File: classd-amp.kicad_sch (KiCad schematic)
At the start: 50 parts, among them Q1 IRF540N, Q2 IRF540N, Q3 IRF540N, Q4 IRF540N, U1 TL072, U2 TL072, U4 LT1016, U5 IR2184, U6 IR2184

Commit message: Added right channel
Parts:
- removed C1: 22u, TerminalBlock_4Ucon:TerminalBlock_4Ucon_1x02_P3.50mm_Horizontal, symbol Device:C
- removed C10, C11, C4, C8, C9: 1n, Capacitor_THT:C_Disc_D4.7mm_W2.5mm_P5.00mm, symbol Device:C
- removed C12, C13, C14: 100n, Capacitor_THT:C_Disc_D3.4mm_W2.1mm_P2.50mm, symbol Device:C
- removed C15, C16: 1u, Capacitor_THT:CP_Radial_D4.0mm_P1.50mm, symbol Device:C_Polarized
- removed C2, C5, C6: 22u, Capacitor_THT:CP_Radial_D8.0mm_P3.50mm, symbol Device:C
- removed C21, C22: 1u, Capacitor_THT:C_Rect_L18.0mm_W11.0mm_P15.00mm_FKS3_FKP3, symbol Device:C
- removed C23, C24: 10u, Capacitor_THT:CP_Radial_D4.0mm_P1.50mm, symbol Device:C_Polarized
- removed D1, D2: 1N4001, Diode_THT:D_DO-41_SOD81_P10.16mm_Horizontal, symbol Device:D
- removed D3, D4, D5, D6: SB140, Diode_THT:D_DO-41_SOD81_P10.16mm_Horizontal, symbol Device:D_Schottky
- removed L1, L2: 33u, Inductor_THT:L_Toroid_Vertical_L17.8mm_W8.1mm_P7.62mm_Bourns_5700, symbol Device:L
- removed Q1, Q2, Q3, Q4: IRF540N, Package_TO_SOT_THT:TO-220-3_Vertical, symbol PCM_Transistor_MOSFET_AKL:IRF540N
- removed R1, R2: 22k, Resistor_THT:R_Axial_DIN0204_L3.6mm_D1.6mm_P7.62mm_Horizontal, symbol Device:R
- removed R10, R11, R12, R9: 4.7, Resistor_THT:R_Axial_DIN0204_L3.6mm_D1.6mm_P7.62mm_Horizontal, symbol Device:R
- removed R13, R14: 10, Resistor_THT:R_Axial_DIN0614_L14.3mm_D5.7mm_P5.08mm_Vertical, symbol Device:R
- removed R3, R4: 47k, Resistor_THT:R_Axial_DIN0204_L3.6mm_D1.6mm_P7.62mm_Horizontal, symbol Device:R
- removed R5, R6: 3.3k, Resistor_THT:R_Axial_DIN0204_L3.6mm_D1.6mm_P7.62mm_Horizontal, symbol Device:R
- removed R7, R8: 100k, Resistor_THT:R_Axial_DIN0204_L3.6mm_D1.6mm_P7.62mm_Horizontal, symbol Device:R
- removed RV1: 1k, Potentiometer_THT:TRIM_3362P-1-253LF, symbol Device:R_Potentiometer_Trim
- removed U1, U2: TL072, PCM_Package_DIP_AKL:DIP-8_W7.62mm, symbol Amplifier_Operational:TL072
- removed U4: LT1016, PCM_Package_DIP_AKL:DIP-8_W7.62mm, symbol Comparator:LT1016
- removed U5, U6: IR2184, PCM_Package_DIP_AKL:DIP-8_W7.62mm, symbol Driver_FET:IR2184
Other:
- added sheet Left Channel (left.kicad_sch)
- added sheet Right Channel (right.kicad_sch)

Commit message: First prototype
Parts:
- added J2: Conn_Coaxial_x2, Connector_Audio:RCA_Stereo_Connector, symbol Connector:Conn_Coaxial_x2
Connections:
- new net GND: J2.3 (EXT)
- new net LIN: J2.2 (IN2)
- new net RIN: J2.1 (IN1)
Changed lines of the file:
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@@
 (kicad_sch (version 20230121) (generator eeschema)
   (paper "A4")
+  (wire (pts (xy 22.86 81.28) (xy 27.94 81.28))
+    (stroke (width 0) (type default))
+  )
+  (wire (pts (xy 27.94 100.33) (xy 30.48 100.33))
+    (stroke (width 0) (type default))
+  )
+  (wire (pts (xy 27.94 81.28) (xy 27.94 85.09))
+    (stroke (width 0) (type default))
+  )
+  (wire (pts (xy 27.94 95.25) (xy 30.48 95.25))
+    (stroke (width 0) (type default))
+  )
+  (wire (pts (xy 22.86 90.17) (xy 22.86 81.28))
+    (stroke (width 0) (type default))
+  )
+  (global_label "LIN" (shape output) (at 30.48 95.25 0) (fields_autoplaced)
+    (effects (font (size 1.27 1.27)) (justify left))
+    (property "Intersheetrefs" "${INTERSHEET_REFS}" (at 36.4286 95.25 0)
+      (effects (font (size 1.27 1.27)) (justify left) hide)
+    )
+  )
+  (global_label "RIN" (shape output) (at 30.48 100.33 0) (fields_autoplaced)
+    (effects (font (size 1.27 1.27)) (justify left))
+    (property "Intersheetrefs" "${INTERSHEET_REFS}" (at 36.6705 100.33 0)
+      (effects (font (size 1.27 1.27)) (justify left) hide)
+    )
+  )
+  (symbol (lib_id "Connector:Conn_Coaxial_x2") (at 22.86 97.79 180) (unit 1)
+    (in_bom yes) (on_board yes) (dnp no) (fields_autoplaced)
+    (property "Reference" "J2" (at 19.05 96.2268 0)
+      (effects (font (size 1.27 1.27)) (justify left))
+    )
+    (property "Value" "Conn_Coaxial_x2" (at 19.05 98.7668 0)
+      (effects (font (size 1.27 1.27)) (justify left) hide)
+    )
+    (property "Footprint" "Connector_Audio:RCA_Stereo_Connector" (at 22.86 95.25 0)
+      (effects (font (size 1.27 1.27)) hide)
+    )
+    (property "Datasheet" " ~" (at 22.86 95.25 0)
+      (effects (font (size 1.27 1.27)) hide)
+    )
+    (pin "1")
+    (pin "2")
+    (pin "3")
+    (instances
+      (project "classd-amp"
+        (path "/4342a3a3-4383-4661-90ac-821979f46c8c"
+          (reference "J2") (unit 1)
+        )
+      )
+    )
+  )
+  (symbol (lib_id "power:GND") (at 27.94 85.09 0) (unit 1)
+    (in_bom yes) (on_board yes) (dnp no) (fields_autoplaced)
+    (property "Reference" "#PWR056" (at 27.94 91.44 0)
+      (effects (font (size 1.27 1.27)) hide)
+    )
+    (property "Value" "GND" (at 27.94 90.17 0)
+      (effects (font (size 1.27 1.27)))
+    )
+    (property "Footprint" "" (at 27.94 85.09 0)
+      (effects (font (size 1.27 1.27)) hide)
+    )
+    (property "Datasheet" "" (at 27.94 85.09 0)
+      (effects (font (size 1.27 1.27)) hide)
+    )
+    (pin "1")
+    (instances
+      (project "classd-amp"
+        (path "/4342a3a3-4383-4661-90ac-821979f46c8c"
+          (reference "#PWR056") (unit 1)
+        )
+      )
+    )
+  )
   (sheet (at 167.64 83.82) (size 110.49 69.85) (fields_autoplaced)
     (stroke (width 0.1524) (type solid))
@@
     )
   )
-  (sheet (at 39.37 115.57) (size 110.49 69.85) (fields_autoplaced)
+  (sheet (at 49.53 107.95) (size 110.49 69.85) (fields_autoplaced)
     (stroke (width 0.1524) (type solid))
     (fill (color 0 0 0 0.0000))
-    (property "Sheetname" "Left Channel" (at 39.37 114.8584 0)
+    (property "Sheetname" "Left Channel" (at 49.53 107.2384 0)
       (effects (font (size 1.27 1.27)) (justify left bottom))
     )
-    (property "Sheetfile" "left.kicad_sch" (at 39.37 186.0046 0)
+    (property "Sheetfile" "left.kicad_sch" (at 49.53 178.3846 0)
       (effects (font (size 1.27 1.27)) (justify left top))
     )
@@
     )
   )
-  (sheet (at 29.464 26.67) (size 82.296 69.85) (fields_autoplaced)
+  (sheet (at 73.914 25.4) (size 82.296 69.85) (fields_autoplaced)
     (stroke (width 0.1524) (type solid))
     (fill (color 0 0 0 0.0000))
-    (property "Sheetname" "Power Supplies" (at 29.464 25.9584 0)
+    (property "Sheetname" "Power Supplies" (at 73.914 24.6884 0)
       (effects (font (size 1.27 1.27)) (justify left bottom))
     )
-    (property "Sheetfile" "power.kicad_sch" (at 29.464 97.1046 0)
+    (property "Sheetfile" "power.kicad_sch" (at 73.914 95.8346 0)
       (effects (font (size 1.27 1.27)) (justify left top))
     )

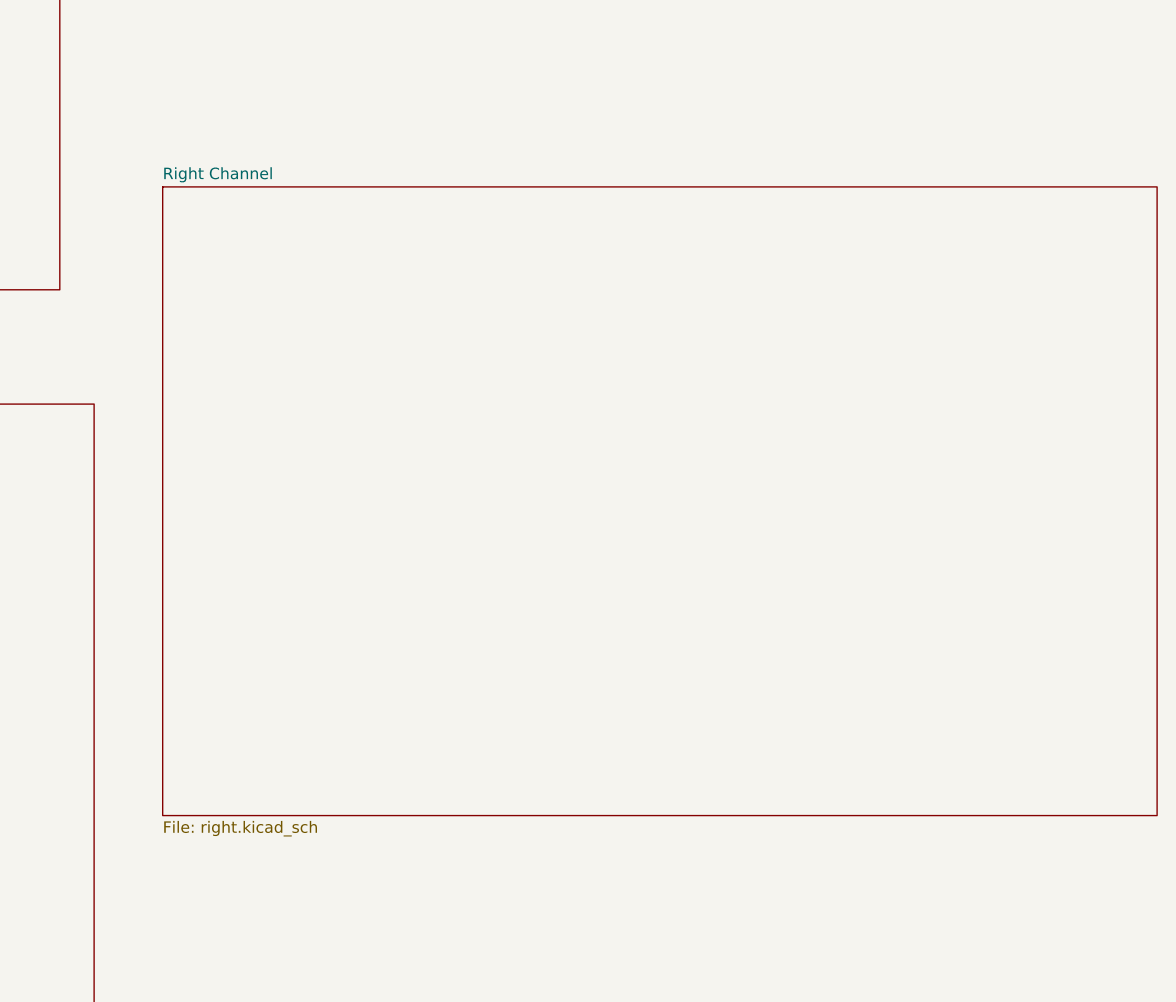
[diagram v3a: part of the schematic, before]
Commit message: Recovered PCB
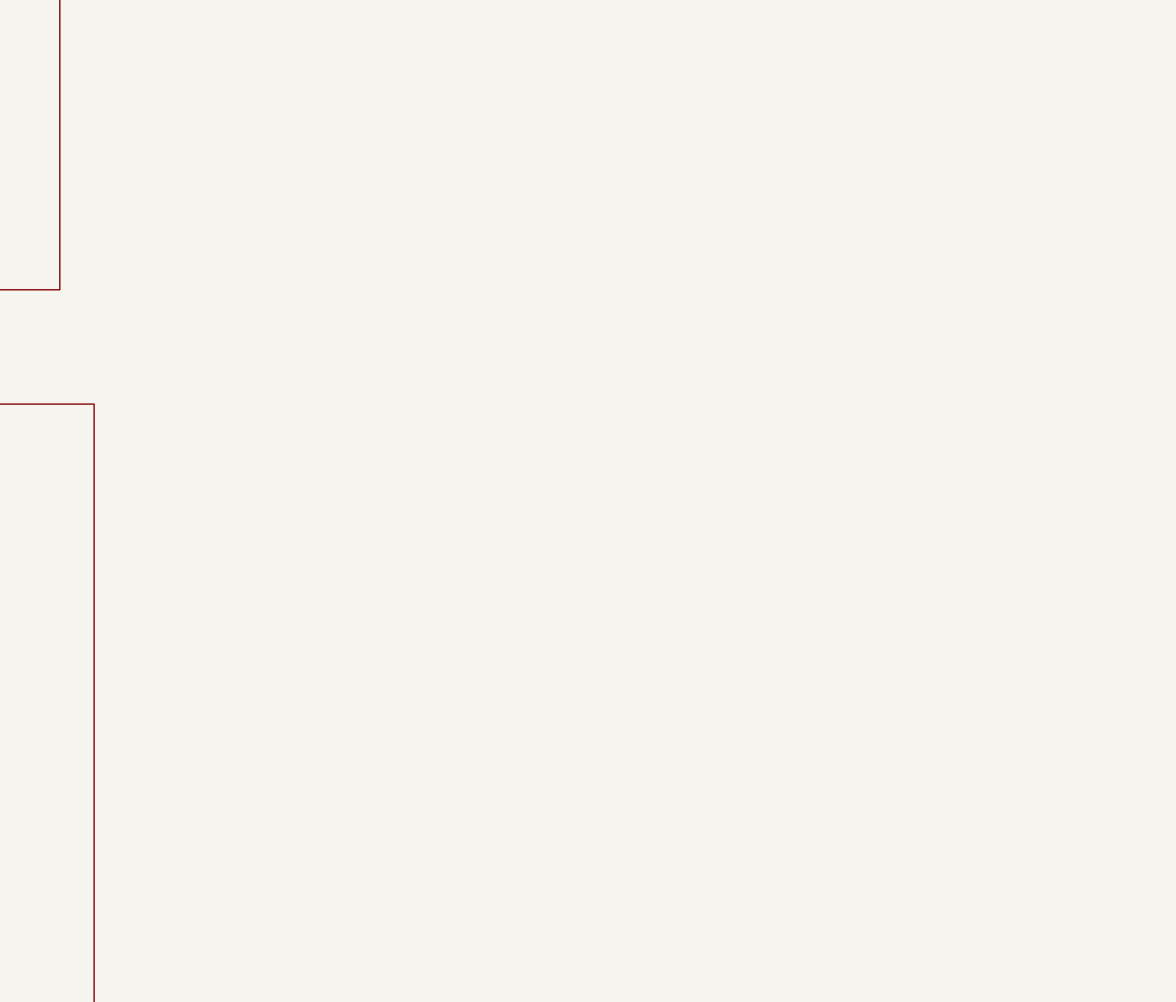
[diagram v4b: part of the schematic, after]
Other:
- removed sheet Right Channel
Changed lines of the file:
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@@
-	)
-	(sheet
-		(at 167.64 83.82)
-		(size 110.49 69.85)
-		(fields_autoplaced yes)
-		(stroke
-			(width 0.1524)
-			(type solid)
-		)
-		(fill
-			(color 0 0 0 0.0000)
-		)
-		(property "Sheetname" "Right Channel"
-			(at 167.64 83.1084 0)
-			(effects
-				(font
-					(size 1.27 1.27)
-				)
-				(justify left bottom)
-			)
-		)
-		(property "Sheetfile" "right.kicad_sch"
-			(at 167.64 154.2546 0)
-			(effects
-				(font
-					(size 1.27 1.27)
-				)
-				(justify left top)
-			)
-		)
-		(instances
-			(project "classd-amp"
-				(path "/4342a3a3-4383-4661-90ac-821979f46c8c"
-					(page "4")
-				)
-			)
-		)
 	)
 	(sheet
